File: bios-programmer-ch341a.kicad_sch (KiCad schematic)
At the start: 22 parts, among them J1 USB_B_Micro, J2 Conn_01x07, J3 Conn_01x07, J4 +Banana+, J5 -Banana-, J6 ZIF16, U1 CH341A, U2 ISO6741, U3 ADUM1252, Y1 Crystal

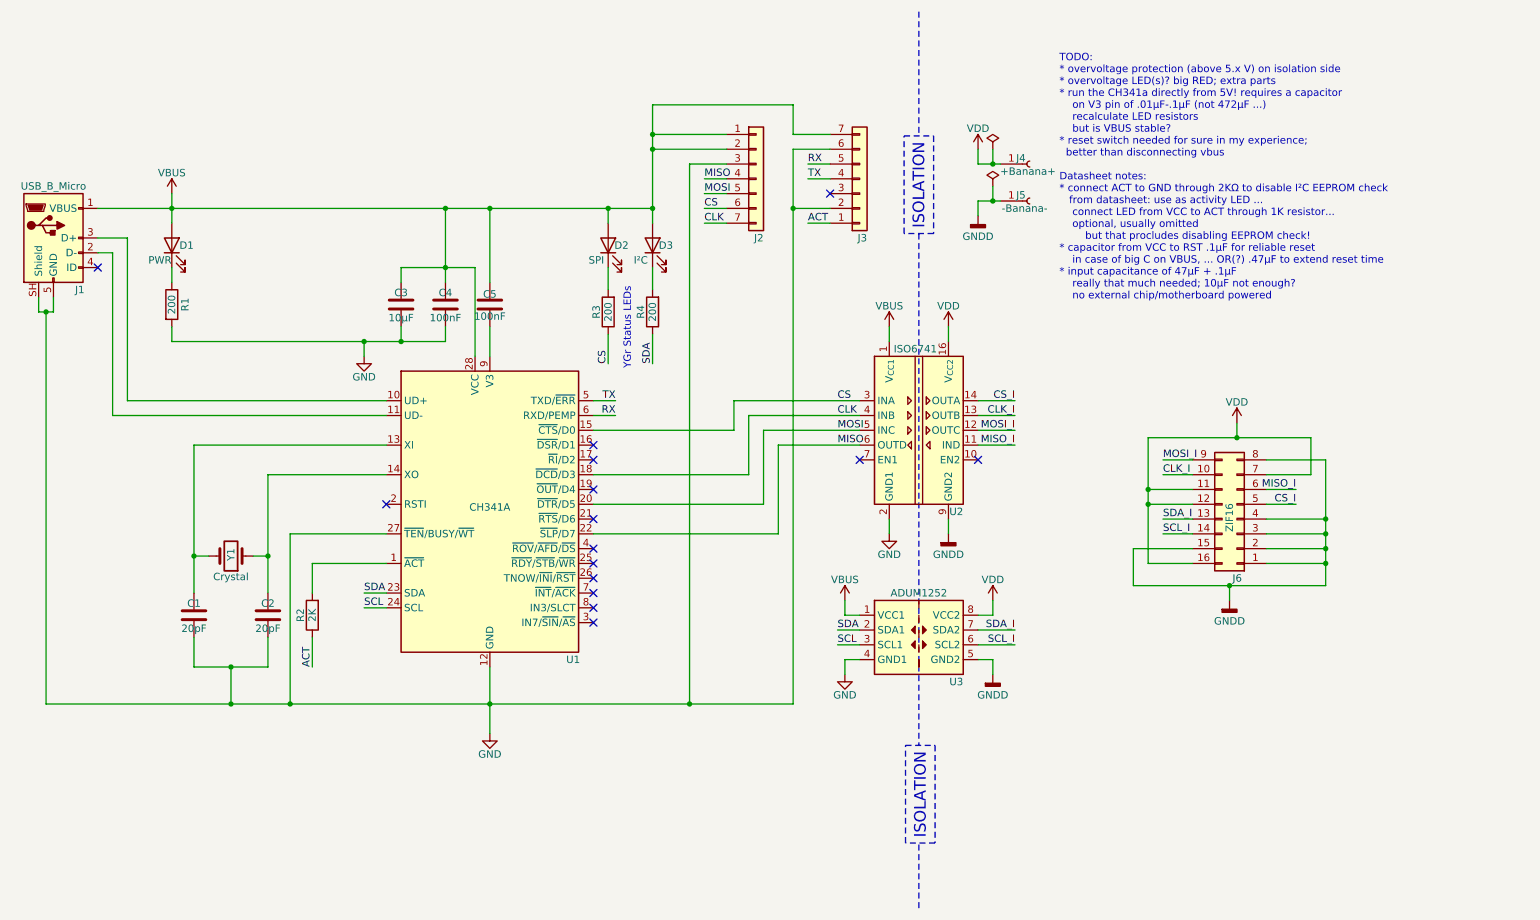
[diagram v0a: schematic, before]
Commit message: Cleanup of tracks and condensing a bit + adding the Ohm symbols again
I cannot resist using correct units.
The layout as it is doesn't cross any signals, at the cost of becoming slightly
more difficult to follow. Then again, it's a simple design and supposed to stay
that way.
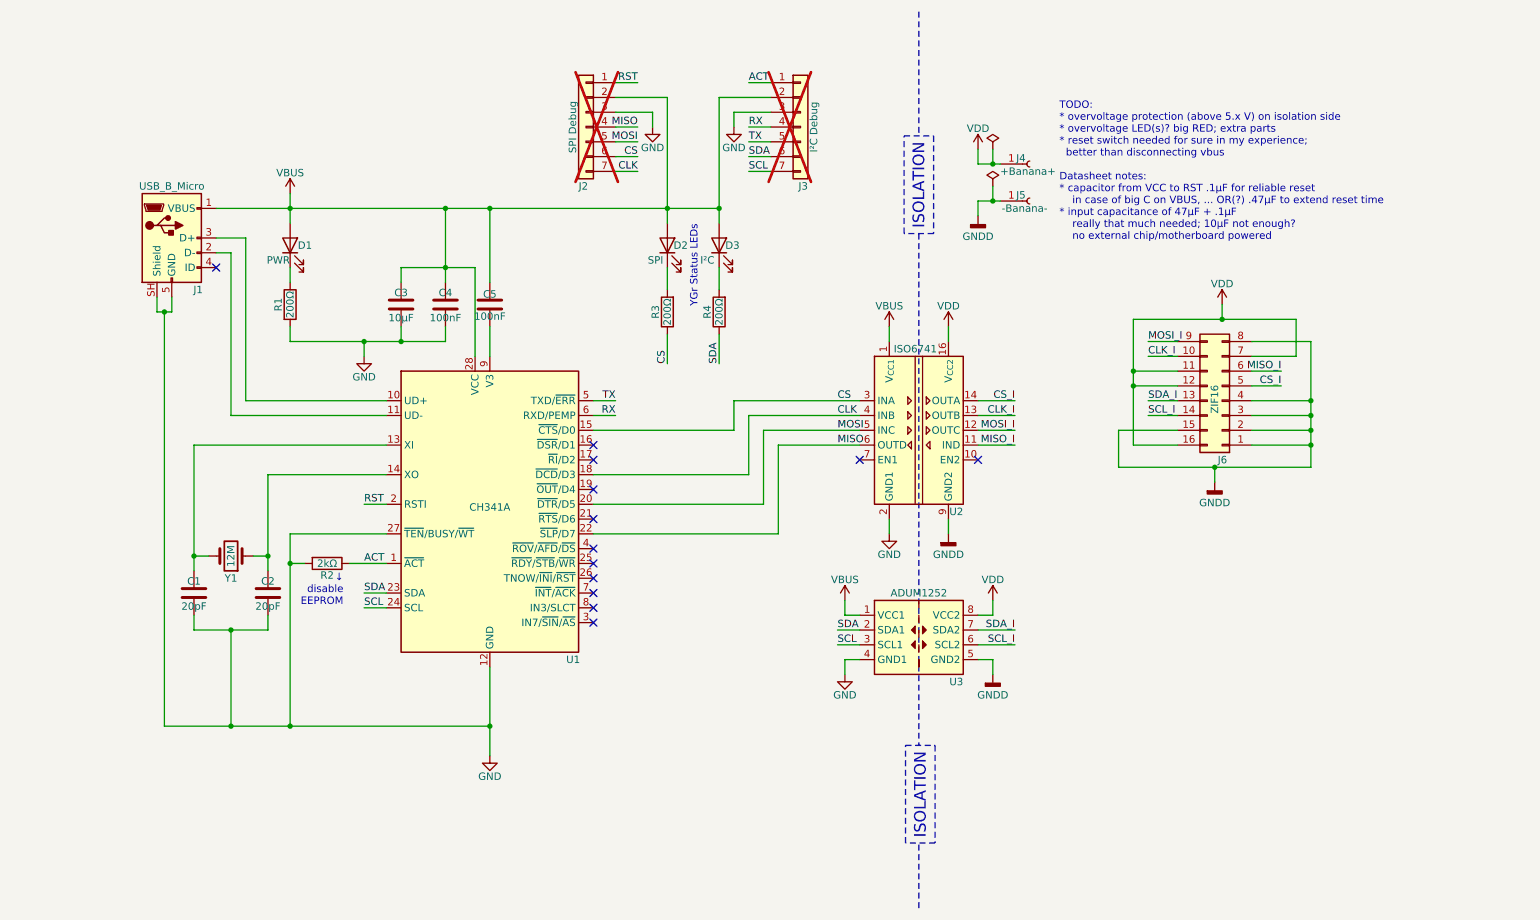
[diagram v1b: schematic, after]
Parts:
- J2: value Conn_01x07 -> SPI Debug; now not fitted
- J3: value Conn_01x07 -> I²C Debug; now not fitted
- R1, R3, R4: value 200 -> 200Ω
- R2: value 2K -> 2kΩ
- Y1: value Crystal -> 12M
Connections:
- net ACT: now also U1.1 (~{ACT})
- net GND: now also J3.3 (Pin_3), R2.2; no longer J3.2 (Pin_2), J3.6 (Pin_6)
- net RX: now also J3.4 (Pin_4); no longer J3.5 (Pin_5)
- net SCL: now also J3.7 (Pin_7)
- net SDA: now also J3.6 (Pin_6)
- net TX: now also J3.5 (Pin_5); no longer J3.4 (Pin_4)
- net VBUS: now also J3.2 (Pin_2); no longer J2.1 (Pin_1), J3.7 (Pin_7)
- net RST: now reaches U1.2 (RSTI)
- net RST: now also J2.1 (Pin_1)
- no-connect marks 15 -> 13
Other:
- note added: "TODO: * overvoltage protection (above 5.x V) on isolation side * overvoltage LED(s)? big RED; extra parts * reset switch needed for sure in my experience; better than disconnecting vbus Datasheet notes: * capacitor from VCC to RST .1µF for reliable reset in case of big C on VBUS, ... OR(?) .47µF to extend reset time * input capacitance of 47µF + .1µF really that much needed; 10µF not enough? no e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"
- note added: "↓ disable EEPROM"
- note removed: "TODO: * overvoltage protection (above 5.x V) on isolation side * overvoltage LED(s)? big RED; extra parts * run the CH341a directly from 5V! requires a capacitor on V3 pin of .01µF-.1µF (not 472µF ...) recalculate LED resistors but is VBUS stable? * reset switch needed for sure in my experience; better than disconnecting vbus Datasheet notes: * connect ACT to GND through 2KΩ to disable I²C EEPROM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"
- moved on the sheet: C1, C2, D1, D2, D3, J1, J6, R1, R2, R3, R4

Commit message: Added a reset switch and removed RST & ACT signals from debug headers
The reset is probably useful, I've had plenty of times that one of these CH341
chips or the chip under programming  stopped responding because something went
wrong with the software.
No need to unplug the USB all the time, reset switches should be more omni-
present.

Those 2 extra signals aren't really needed for debugging if there's a switch,
ACT was barely useful anyway. Also note that these parts are DNP anyway.
And I might turn it into 2mm or even 1mm pitches if need be. I should check up
on test point (those clip-on ones) sizes before I do so though.
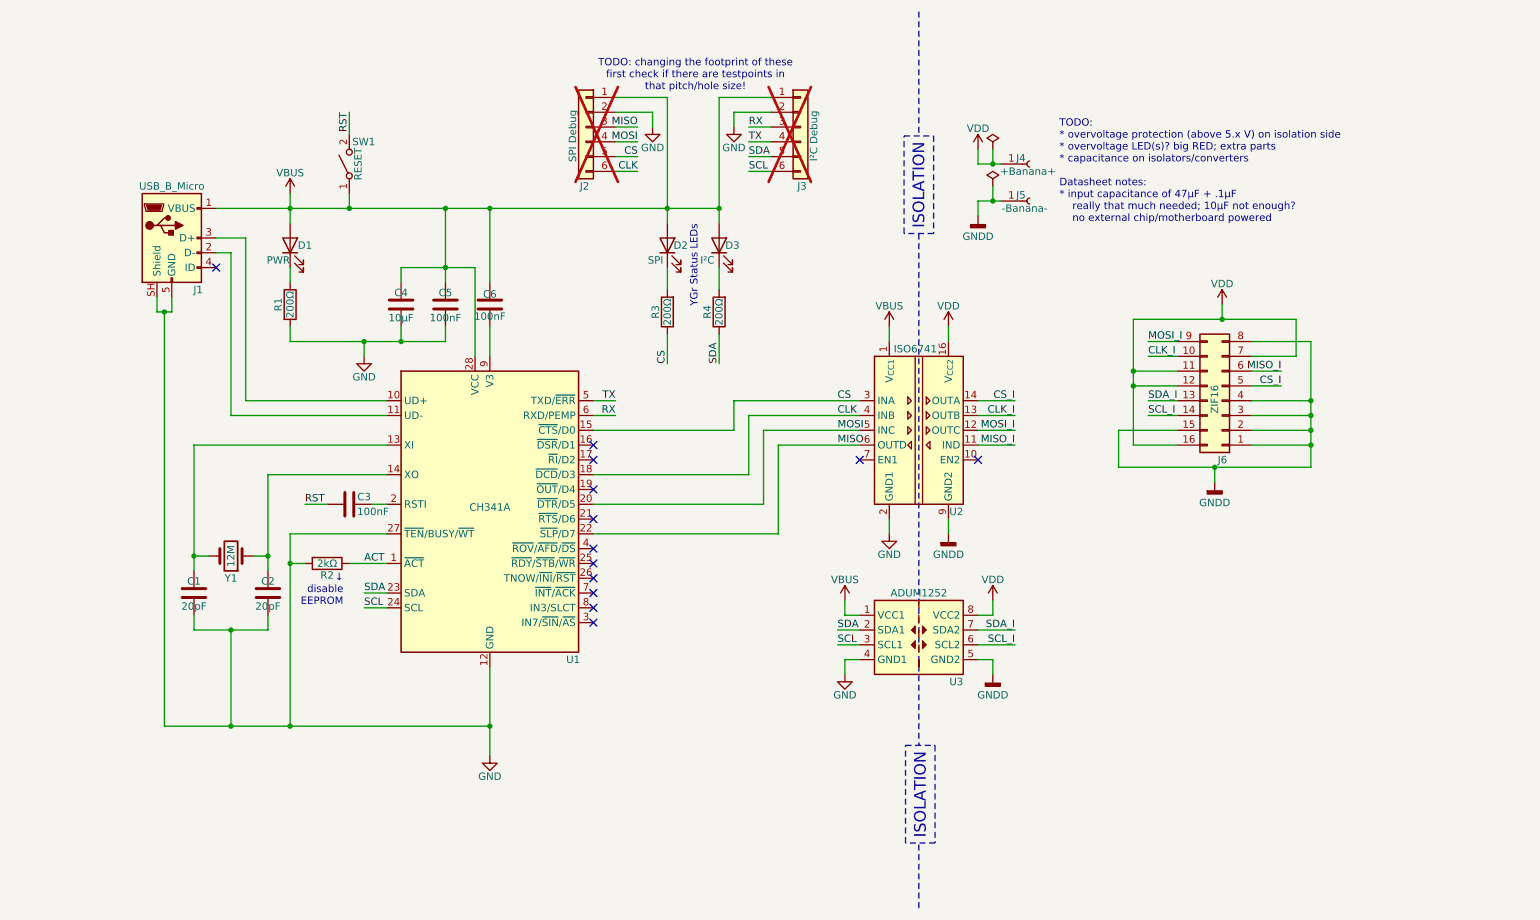
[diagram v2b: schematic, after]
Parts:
- removed J2: SPI Debug, Connector_PinHeader_2.54mm:PinHeader_1x07_P2.54mm_Vertical, symbol Connector_Generic:Conn_01x07
- removed J3: I²C Debug, Connector_PinHeader_2.54mm:PinHeader_1x07_P2.54mm_Vertical, symbol Connector_Generic:Conn_01x07
- added C3: 100nF, Capacitor_SMD:C_0603_1608Metric_Pad1.08x0.95mm_HandSolder, symbol Device:C
- added J2: SPI Debug, Connector_PinSocket_2.54mm:PinSocket_1x06_P2.54mm_Vertical, symbol Connector_Generic:Conn_01x06
- added J3: I²C Debug, Connector_PinSocket_2.54mm:PinSocket_1x06_P2.54mm_Vertical, symbol Connector_Generic:Conn_01x06
- added SW1: RESET, Button_Switch_SMD:SW_SPST_TL3342, symbol Switch:SW_SPST
- renumbered C3 to C4, C4 to C5, C5 to C6
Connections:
- net CLK: now also J2.6 (Pin_6)
- net CS: now also J2.5 (Pin_5)
- net GND: now also J2.2 (Pin_2), J3.2 (Pin_2)
- net MISO: now also J2.3 (Pin_3)
- net MOSI: now also J2.4 (Pin_4)
- net RST: now also C3.2, SW1.2 (B); no longer U1.2 (RSTI)
- net RX: now also J3.3 (Pin_3)
- net SCL: now also J3.6 (Pin_6)
- net SDA: now also J3.5 (Pin_5)
- net TX: now also J3.4 (Pin_4)
- net VBUS: now also J2.1 (Pin_1), J3.1 (Pin_1), SW1.1 (A)
- new net: C3.1, U1.2 (RSTI)
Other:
- note added: "TODO: * overvoltage protection (above 5.x V) on isolation side * overvoltage LED(s)? big RED; extra parts * capacitance on isolators/converters Datasheet notes: * input capacitance of 47µF + .1µF really that much needed; 10µF not enough? no external chip/motherboard powered"
- note added: "TODO: changing the footprint of these first check if there are testpoints in that pitch/hole size!"
- note removed: "TODO: * overvoltage protection (above 5.x V) on isolation side * overvoltage LED(s)? big RED; extra parts * reset switch needed for sure in my experience; better than disconnecting vbus Datasheet notes: * capacitor from VCC to RST .1µF for reliable reset in case of big C on VBUS, ... OR(?) .47µF to extend reset time * input capacitance of 47µF + .1µF really that much needed; 10µF not enough? no e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"

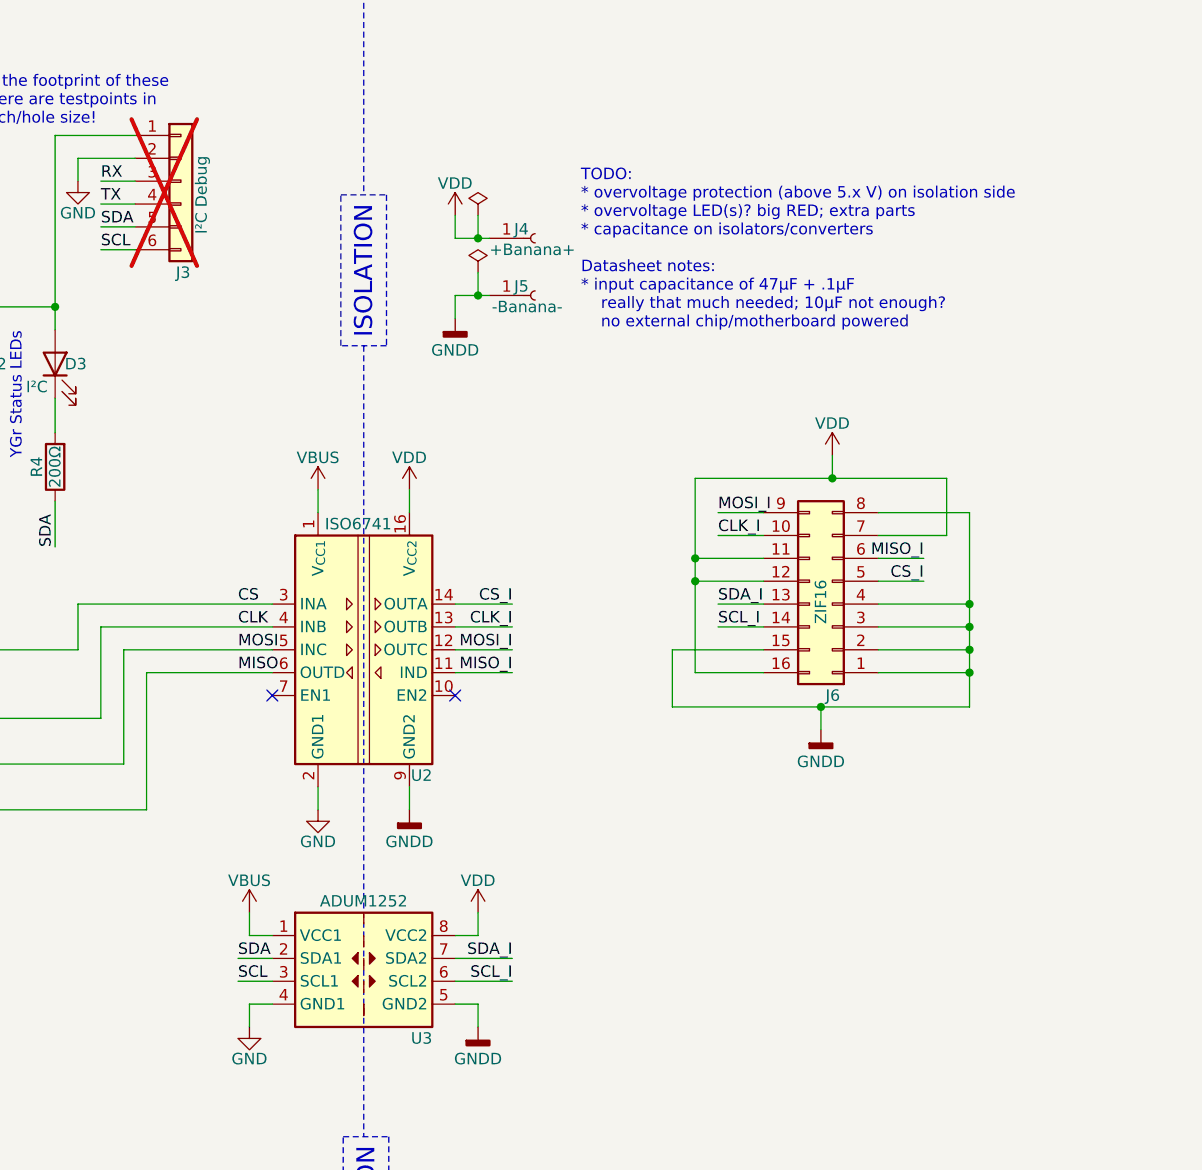
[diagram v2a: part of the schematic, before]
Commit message: Isolators input (VCC) capacitance
Added the required input capacitance on both isolators as specified in the
datasheet.
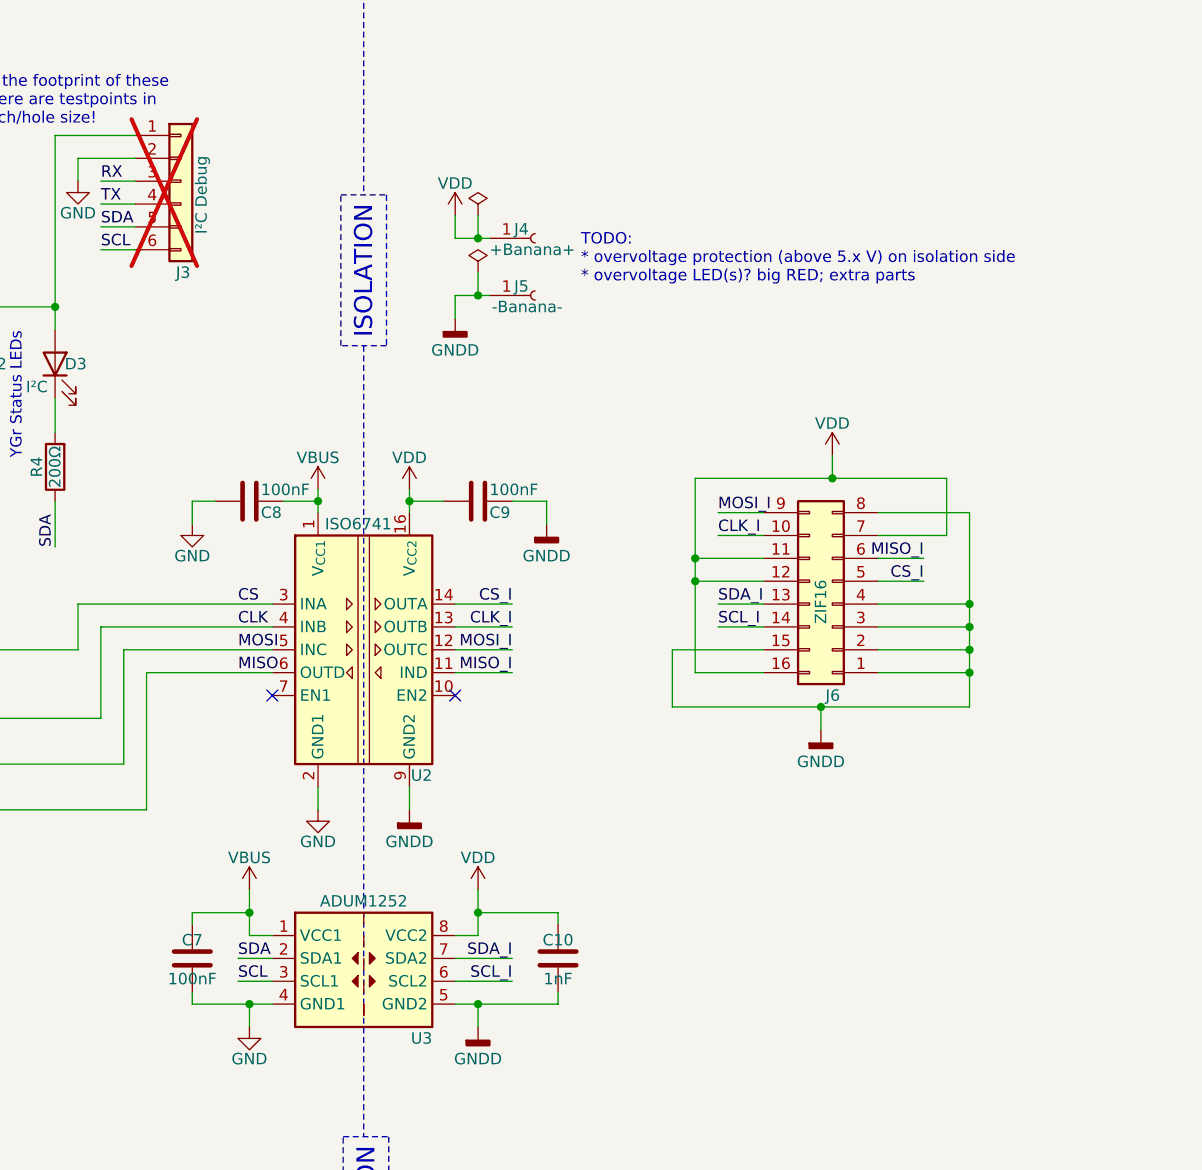
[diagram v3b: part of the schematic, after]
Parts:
- added C10: 1nF, Capacitor_SMD:C_0603_1608Metric_Pad1.08x0.95mm_HandSolder, symbol Device:C
- added C7, C8, C9: 100nF, Capacitor_SMD:C_0603_1608Metric_Pad1.08x0.95mm_HandSolder, symbol Device:C
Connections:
- net GND: now also C7.2, C8.2
- net GNDD: now also C10.2, C9.1
- net VBUS: now also C7.1, C8.1
- net VDD: now also C10.1, C9.2
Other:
- note added: "TODO: * overvoltage protection (above 5.x V) on isolation side * overvoltage LED(s)? big RED; extra parts"
- note removed: "TODO: * overvoltage protection (above 5.x V) on isolation side * overvoltage LED(s)? big RED; extra parts * capacitance on isolators/converters Datasheet notes: * input capacitance of 47µF + .1µF really that much needed; 10µF not enough? no external chip/motherboard powered"
